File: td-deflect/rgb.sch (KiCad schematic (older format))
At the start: 67 parts, among them J5 DB15_Female_HighDensity, U11 24LC08

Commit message: annotate
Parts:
- removed C? (x2): 0.1, symbol Device:C
- removed C? (x2): 2.2uF, symbol Device:CP
- removed R? (x3): 5.5k, symbol Device:R
- removed R? (x2): 560, symbol Device:R
- removed R?: 2.7k, symbol Device:R
- removed R? (x2): 220, symbol Device:R
- removed RV? (x2): 3.3k, symbol Device:R_POT
- added C51, C52: 0.1, symbol Device:C
- added C53, C55: 2.2uF, symbol Device:CP
- added R51, R58, R61: 5.5k, symbol Device:R
- added R60, R64: 560, symbol Device:R
- added R62: 2.7k, symbol Device:R
- added R65, R66: 220, symbol Device:R
- added RV4, RV5: 3.3k, symbol Device:R_POT
- gave numbers to parts that had none: 51
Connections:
- net +12V: now also R51.1, R58.1, R61.1
- net GND: now also C51.2, C52.2, C53.2, C55.2, R60.2, R62.2, R64.2
- net at U18.24 (G_HOLD): now also C55.1
- net at U18.28 (R_HOLD): now also C53.1
- net at U18.4 (R_SUB_CONTRAST): now also R65.1
- net at U18.8 (G_SUB_CONTRAST): now also R66.1
- net at C48.2, R55.1: now also R60.1
- net at C49.1, R56.1: now also R64.1
- net at R67.2: now also RV5.2
- net at RV2.1: now also R51.2
- net at RV2.2: now also R65.2
- net at R73.2, RV7.2: now also C51.1
- net at R74.2, RV8.2: now also C52.1
- net at R59.1: now also RV4.3
- new net: R61.2, RV5.1
- new net: R62.1, RV5.3
- new net: R58.2, RV4.1
- new net: R66.2, RV4.2
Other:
- moved on the sheet: C52, C55, R58, R62, R64, R65, RV5

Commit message: more stuff
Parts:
- added R90, R91, R92, R93: 75, Resistor_SMD:R_0805_2012Metric_Pad1.15x1.40mm_HandSolder, symbol Device:R
- added SW1: SW_DIP_x04, Button_Switch_THT:SW_DIP_SPSTx04_Slide_9.78x12.34mm_W7.62mm_P2.54mm, symbol Switch:SW_DIP_x04
- C47, C51, C52, C54: value 0.1 -> 0.1uF; footprint (none) -> Capacitor_SMD:C_0805_2012Metric_Pad1.15x1.40mm_HandSolder
- C48, C49, C50: footprint (none) -> Capacitor_SMD:C_1206_3216Metric_Pad1.42x1.75mm_HandSolder; Digikey (none) -> 1276-3064-1-ND; Voltage (none) -> 6.3V
- C53, C55, C56: footprint (none) -> Capacitor_SMD:C_0805_2012Metric_Pad1.15x1.40mm_HandSolder; symbol Device:CP -> Device:C
- C57: footprint (none) -> Capacitor_SMD:C_0805_2012Metric_Pad1.15x1.40mm_HandSolder
- C58: value C -> 0.1uF; footprint (none) -> Capacitor_SMD:C_0805_2012Metric_Pad1.15x1.40mm_HandSolder
- J7: footprint (none) -> Connector_Phoenix_MC:PhoenixContact_MCV_1,5_8-G-3.5_1x08_P3.50mm_Vertical
- R51, R52, R53, R54, R55, R56, R57, R58, R59, R60, R61, R62, R63, R64, R65, R66, R67, R68, R69, R70, R71, R72, R73, R74, R75, R76, R77, R78, R79, R80, R81, R82, R83, R84, R85, R86, R87, R88, R89: footprint (none) -> Resistor_SMD:R_0805_2012Metric_Pad1.15x1.40mm_HandSolder
- RV2, RV3, RV4, RV5, RV6, RV7, RV8, RV9: footprint (none) -> Potentiometer_THT:Potentiometer_Bourns_3386P_Vertical
- U18: footprint (none) -> td-deflect:DIP-30_600_ELL
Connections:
- net GND: now also SW1.5, SW1.6, SW1.7, SW1.8
- net blue_vga: now also R92.2
- net green_vga: now also R91.2
- net hsync_vga: now also R93.2
- net red_vga: now also R90.2
- new net: R90.1, SW1.1
- new net: R91.1, SW1.2
- new net: R92.1, SW1.3
- new net: R93.1, SW1.4

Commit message: asdf
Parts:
- added C59: 0.1uF, Capacitor_SMD:C_0805_2012Metric_Pad1.15x1.40mm_HandSolder, symbol Device:C
- added C60: 220uF, Capacitor_THT:CP_Radial_D8.0mm_P3.50mm, symbol Device:CP
- added D6, D7, D8: BAT54S, Package_TO_SOT_SMD:SOT-23, symbol Diode:BAT54S
- added J16: Conn_01x06_Male, Connector_JST:JST_EH_B6B-EH-A_1x06_P2.50mm_Vertical, symbol Connector:Conn_01x06_Male
- added J17: Conn_01x06_Male, Connector_JST:JST_XH_B6B-XH-A_1x06_P2.50mm_Vertical, symbol Connector:Conn_01x06_Male
- added R94: 33k, Resistor_SMD:R_0805_2012Metric_Pad1.15x1.40mm_HandSolder, symbol Device:R
- added R95: 220, Resistor_SMD:R_0805_2012Metric_Pad1.15x1.40mm_HandSolder, symbol Device:R
- added RV10: 10k, Potentiometer_THT:Potentiometer_Bourns_3386P_Vertical, symbol Device:R_POT
- added U20: 74LVC1GU04DRL, Package_TO_SOT_SMD:SOT-553, symbol 74xGxx:74LVC1GU04DRL
- C47, C51, C52, C54, C58: Digikey (none) -> 1276-1099-1-ND
- C48, C49, C50: Digikey 1276-3064-1-ND -> 1276-3064-1-ND
- C53, C55, C56: Digikey (none) -> 1276-2953-1-ND; Voltage (none) -> 25V
- C57: Digikey (none) -> 1276-1066-1-ND; Voltage (none) -> 25V
- J5: Digikey (none) -> AE11024-ND
- J7: footprint Connector_Phoenix_MC:PhoenixContact_MCV_1,5_8-G-3.5_1x08_P3.50mm_Vertical -> Connector_JST:JST_PH_B8B-PH-K_1x08_P2.00mm_Vertical; Digikey (none) -> 455-1723-ND
- Q14, Q15, Q16: Digikey (none) -> BC847BLT3GOSCT-ND
- R51, R58, R61: value 5.5k -> 6.8k
- R53: value 5.5k -> 0
- R54: value 2.7k -> 2.2k
- R55, R56, R57: value 1 -> 1.5k
- R63: value 1k -> 0
- RV2, RV4, RV5: value 3.3k -> 2.7k; Digikey (none) -> 3386P-502TLF-ND
- RV3: value 3.3k -> 2k; Digikey (none) -> 3386P-502TLF-ND
- RV6, RV7, RV8, RV9: value 3.3k -> 1k; Digikey (none) -> 3386P-502TLF-ND
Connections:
- net +12V: now also J7.1 (Pin_1), J17.1 (Pin_1), RV10.1
- net +3V3: now also U20.5 (VCC)
- net GND: now also C59.2, C60.2, D6.1, D7.1, D8.1, J16.4 (Pin_4), J17.6 (Pin_6), RV10.3, U20.3 (GND)
- net backporch: now also U20.2; no longer U18.15 (CLAMP_PULSE)
- net blue_vga: now also J16.3 (Pin_3)
- net green_vga: now also J16.2 (Pin_2)
- net hsync_vga: now also J16.5 (Pin_5)
- net red_vga: now also J16.1 (Pin_1)
- net at RV3.2: now also R94.2; no longer U18.14 (CONTRAST)
- net at R82.2, R83.1, R84.1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: now also C60.1, D6.2, D7.2, D8.2
- net r_yoke: now reaches J7.8 (Pin_8), R86.1
- net r_yoke: now also D6.3, J17.2 (Pin_2)
- net g_yoke: now reaches J7.6 (Pin_6), R87.1
- net g_yoke: now also D7.3, J17.3 (Pin_3)
- net b_yoke: now reaches J7.4 (Pin_4), R88.1
- net b_yoke: now also D8.3, J17.4 (Pin_4)
- net hsync renamed HSYNC_UC
- net oddeven renamed ODDEVEN_UC
- net vsync renamed VSYNC_UC
- net vsync_vga renamed VSYNC_VGA_UC
- net VSYNC_VGA_UC: now also J16.6 (Pin_6)
- new net: R94.1, R95.2
- new net: C59.1, R95.1, U18.14 (CONTRAST)
- new net: U18.15 (CLAMP_PULSE), U20.4
- new net sub_brightness: J17.5 (Pin_5), RV10.2
- no-connect marks 0 -> 8
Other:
- moved on the sheet: J5, J7, R90, R91, R92, R93, SW1, U11

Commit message: asdf
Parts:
- Q14, Q15, Q16: Digikey BC847BLT3GOSCT-ND -> BC847BLT3GOSCT-ND
- R51, R58, R61: Digikey (none) -> 311-6.80KCRCT-ND
- R52, R59, R62: Digikey (none) -> 311-2.70KCRCT-ND
- R53, R63: Digikey (none) -> 311-0.0ARCT-ND
- R54: Digikey (none) -> 311-2.20KCRCT-ND
- R55, R56, R57: Digikey (none) -> 311-1.50KCRCT-ND
- R60, R64, R68: Digikey (none) -> 311-560CRCT-ND
- R65, R66, R67, R82, R95: Digikey (none) -> 311-220CRCT-ND
- R69, R73, R74, R75: Digikey (none) -> 311-47.0KCRCT-ND
- R70, R71, R72, R76, R77, R78: Digikey (none) -> 311-1.00KCRCT-ND
- R79, R80, R81, R86, R87, R88: Digikey (none) -> 311-47.0CRCT-ND
- R83, R84, R85: Digikey (none) -> 311-470CRCT-ND
- R89: Digikey (none) -> 311-1.00CRCT-ND
- R90, R91, R92, R93: Digikey (none) -> 311-75.0CRCT-ND
- R94: Digikey (none) -> 311-33.0CRCT-ND
- RV10: Digikey 3386P-502TLF-ND -> 3386F-103LF-ND
- RV2, RV3, RV4, RV5: Digikey 3386P-502TLF-ND -> 3386F-202LF-ND
- RV6, RV7, RV8, RV9: Digikey 3386P-502TLF-ND -> 3386P-102LF-ND
- SW1: Digikey (none) -> CT2064-ND
- U11: Digikey (none) -> 24LC08BT/SNCT-ND
- U19: Digikey (none) -> LMH1980MM/NOPBCT-ND
- U20: Digikey (none) -> 296-18657-1-ND

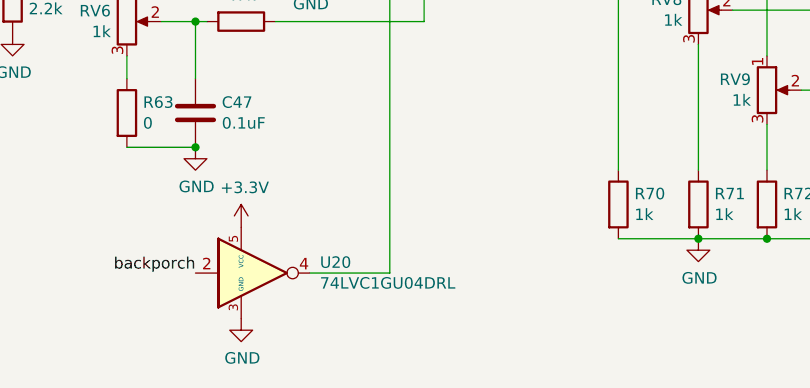
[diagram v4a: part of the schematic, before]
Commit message: Fix some part #s
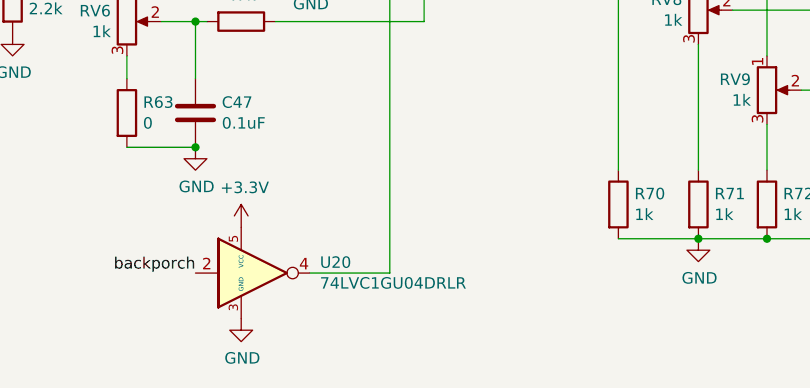
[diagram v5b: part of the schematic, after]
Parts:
- U20: value 74LVC1GU04DRL -> 74LVC1GU04DRLR; Digikey 296-18657-1-ND -> 296-18657-1-ND
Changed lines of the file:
@@
 P 2100 7300
 F 0 "U20" H 2444 7346 50  0000 L CNN
-F 1 "74LVC1GU04DRL" H 2444 7255 50  0000 L CNN
+F 1 "74LVC1GU04DRLR" H 2444 7255 50  0000 L CNN
 F 2 "Package_TO_SOT_SMD:SOT-553" H 2100 7050 50  0001 C CNN
 F 3 "http://www.ti.com/lit/ds/symlink/sn74lvc1gu04.pdf" H 2025 7300 50  0001 C CNN
-F 4 "296-18657-1-ND" H 2100 7300 50  0001 C CNN "Digikey"
+F 4 " 296-18657-1-ND" H 2100 7300 50  0001 C CNN "Digikey"
 	1    2100 7300
 	1    0    0    -1
